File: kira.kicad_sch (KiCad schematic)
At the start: 41 parts, among them J1 USB_C_Receptacle_USB2.0, J2 SWD, SW37 SW_Push, U1 RP2040, U2 XC6206PxxxMR, U3 W25Q128JVS, U4 USBLC6-2SC6, Y1 12MHz

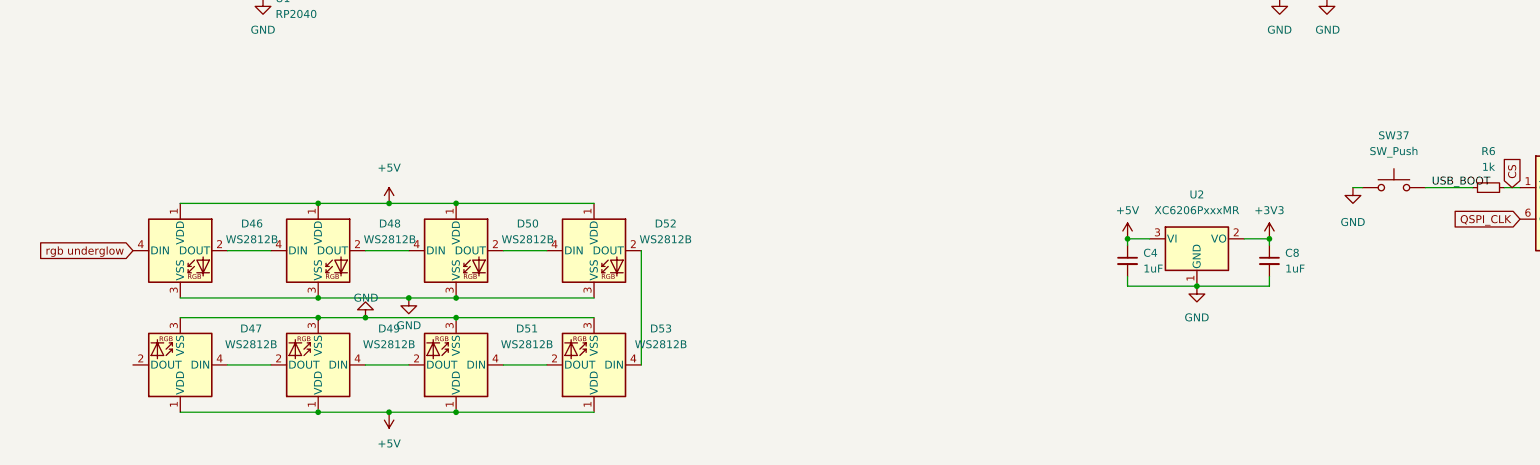
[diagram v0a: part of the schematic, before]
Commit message: removed underglow, cleaned some routing, fixed errors
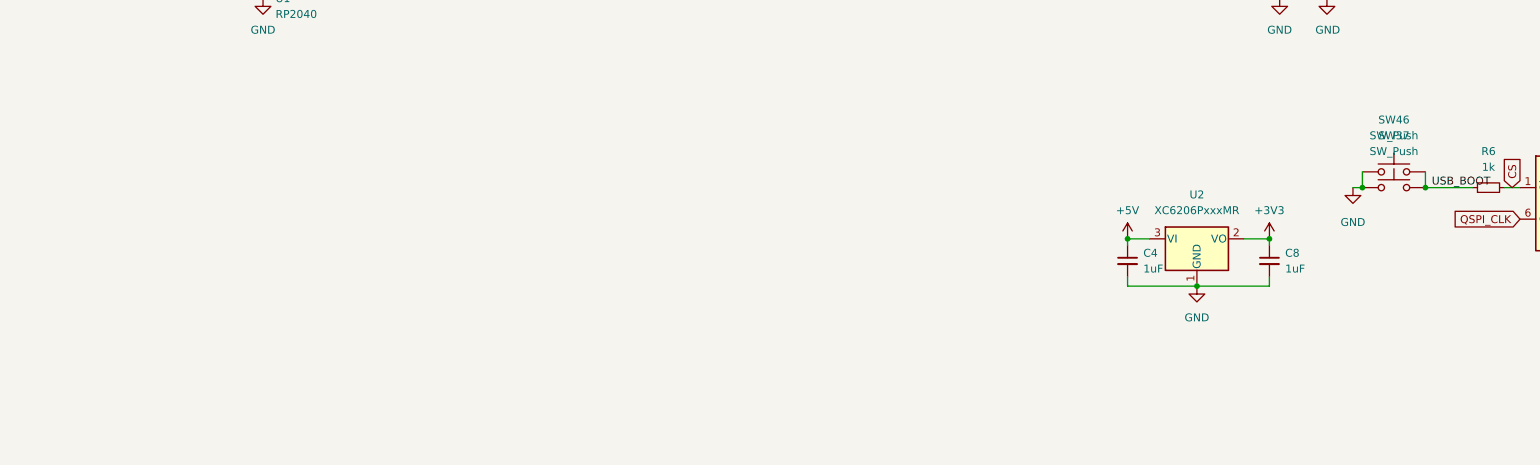
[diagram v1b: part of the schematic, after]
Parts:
- removed D46, D47, D48, D49, D50, D51, D52, D53: WS2812B, CrumpPrints:WS2812-2020, symbol LED:WS2812B
- added SW46: SW_Push, Keebio-Parts:SW_SPST_TL3342, symbol Switch:SW_Push
- SW37: footprint Connector_PinSocket_2.54mm:PinSocket_1x02_P2.54mm_Vertical -> Connector_PinHeader_2.00mm:PinHeader_1x02_P2.00mm_Vertical; now left out of the parts list
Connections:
- net GND: now also SW46.1
- net USB_BOOT: now also SW46.2

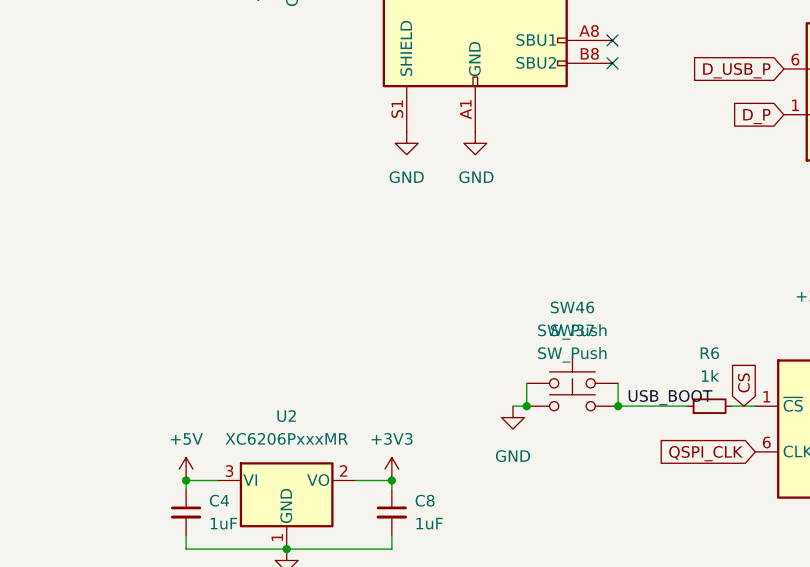
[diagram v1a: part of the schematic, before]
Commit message: silkscreen edited
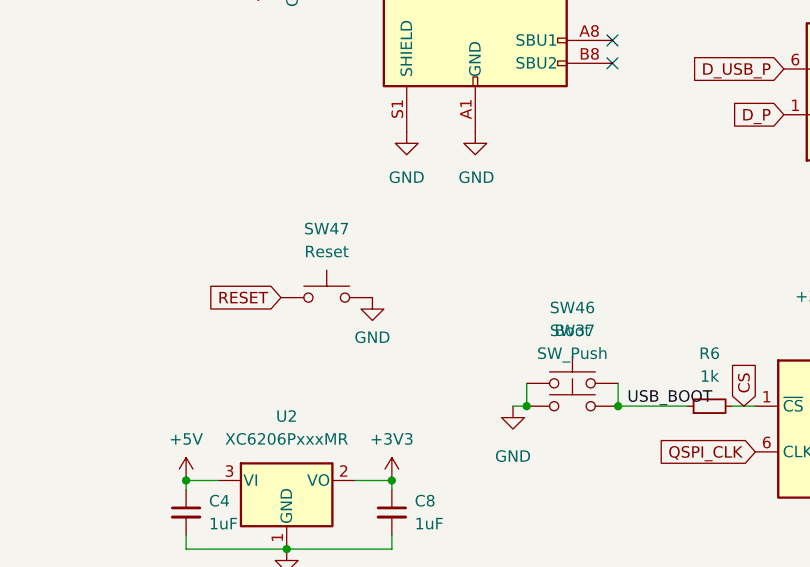
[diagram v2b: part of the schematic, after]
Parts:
- added SW47: Reset, Keebio-Parts:SW_SPST_TL3342, symbol Switch:SW_Push
- SW46: value SW_Push -> Boot
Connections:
- net GND: now also SW47.2
- net RESET: now also SW47.1
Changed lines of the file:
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@@
+    )
+  )
+  (global_label "RESET" (shape input) (at 196.215 133.35 180) (fields_autoplaced)
+    (effects (font (size 1.27 1.27)) (justify right))
+    (property "Intersheet References" "${INTERSHEET_REFS}" (id 0) (at 188.0567 133.2706 0)
+      (effects (font (size 1.27 1.27)) (justify right) hide)
     )
   )
@@
     )
     (property "Datasheet" "" (id 3) (at 217.805 114.935 0)
+      (effects (font (size 1.27 1.27)) hide)
+    )
+    (pin "1")
+  )
+  (symbol (lib_id "power:GND") (at 206.375 133.35 0) (unit 1)
+    (in_bom yes) (on_board yes) (fields_autoplaced)
+    (property "Reference" "#PWR0131" (id 0) (at 206.375 139.7 0)
+      (effects (font (size 1.27 1.27)) hide)
+    )
+    (property "Value" "GND" (id 1) (at 206.375 137.795 0))
+    (property "Footprint" "" (id 2) (at 206.375 133.35 0)
+      (effects (font (size 1.27 1.27)) hide)
+    )
+    (property "Datasheet" "" (id 3) (at 206.375 133.35 0)
       (effects (font (size 1.27 1.27)) hide)
     )
@@
     (pin "2")
   )
+  (symbol (lib_id "Switch:SW_Push") (at 201.295 133.35 0) (unit 1)
+    (in_bom yes) (on_board yes) (fields_autoplaced)
+    (property "Reference" "SW47" (id 0) (at 201.295 125.73 0))
+    (property "Value" "Reset" (id 1) (at 201.295 128.27 0))
+    (property "Footprint" "Keebio-Parts:SW_SPST_TL3342" (id 2) (at 201.295 128.27 0)
+      (effects (font (size 1.27 1.27)) hide)
+    )
+    (property "Datasheet" "~" (id 3) (at 201.295 128.27 0)
+      (effects (font (size 1.27 1.27)) hide)
+    )
+    (pin "1")
+    (pin "2")
+  )
   (symbol (lib_id "Device:C_Small") (at 185.674 157.226 0) (unit 1)
     (in_bom yes) (on_board yes) (fields_autoplaced)
@@
     (in_bom yes) (on_board yes) (fields_autoplaced)
     (property "Reference" "SW46" (id 0) (at 228.6 134.493 0))
-    (property "Value" "SW_Push" (id 1) (at 228.6 137.033 0))
+    (property "Value" "Boot" (id 1) (at 228.6 137.033 0))
     (property "Footprint" "Keebio-Parts:SW_SPST_TL3342" (id 2) (at 228.6 137.795 0)
       (effects (font (size 1.27 1.27)) hide)
@@
       (reference "#PWR0130") (unit 1) (value "GND") (footprint "")
     )
+    (path "/06dd8140-d842-4d91-a09d-19f94dcd5335"
+      (reference "#PWR0131") (unit 1) (value "GND") (footprint "")
+    )
     (path "/0ddedf06-cea5-4a1f-bea2-2a45031a82ea"
       (reference "C1") (unit 1) (value "1uF") (footprint "Capacitor_SMD:C_0402_1005Metric")
@@
     )
     (path "/c0879072-e435-401b-8624-0b44d019e717"
-      (reference "SW46") (unit 1) (value "SW_Push") (footprint "Keebio-Parts:SW_SPST_TL3342")
+      (reference "SW46") (unit 1) (value "Boot") (footprint "Keebio-Parts:SW_SPST_TL3342")
+    )
+    (path "/3fdd5214-4d43-4399-afca-8243e6545b7e"
+      (reference "SW47") (unit 1) (value "Reset") (footprint "Keebio-Parts:SW_SPST_TL3342")
     )
     (path "/f45907fd-0590-42cd-94d3-1afdfd6a497f"

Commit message: quick schematics cleanup
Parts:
- removed SW37: SW_Push, Connector_PinHeader_2.00mm:PinHeader_1x02_P2.00mm_Vertical, symbol Switch:SW_Push
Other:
- moved on the sheet: C1, C2, C3, C5, C6, R7, SW46, Y1

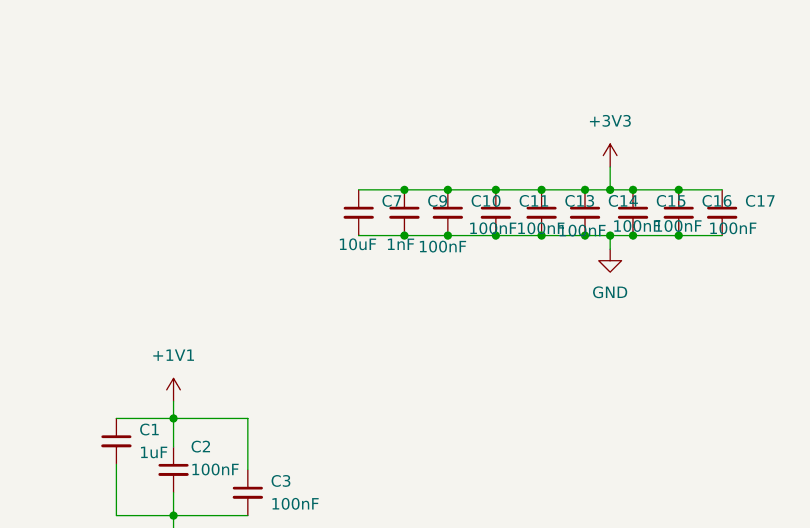
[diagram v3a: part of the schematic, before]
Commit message: started BOM, corrected schematic component value
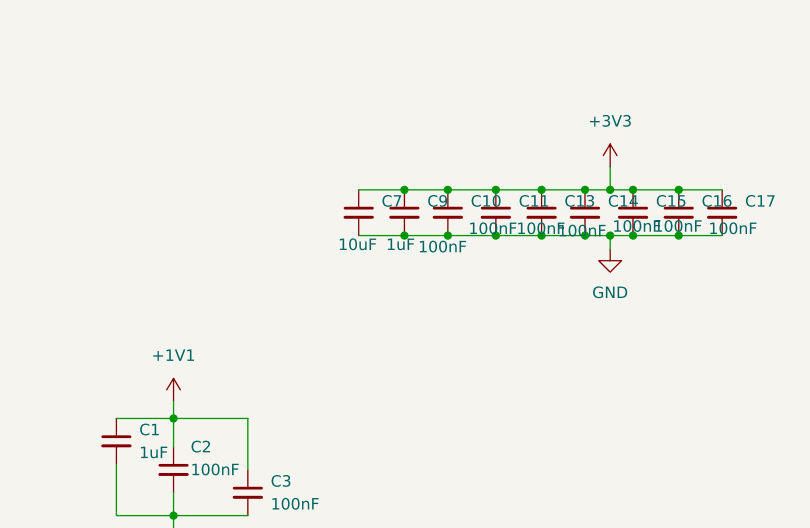
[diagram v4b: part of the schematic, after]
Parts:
- C9: value 1nF -> 1uF
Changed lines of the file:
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@@
       (effects (font (size 1.27 1.27)) (justify left))
     )
-    (property "Value" "1nF" (id 1) (at 151.257 34.671 0)
+    (property "Value" "1uF" (id 1) (at 151.257 34.671 0)
       (effects (font (size 1.27 1.27)) (justify left))
     )
@@
     )
     (path "/2d7efb7f-ebd2-47b3-9634-ae056645508c"
-      (reference "C9") (unit 1) (value "1nF") (footprint "Capacitor_SMD:C_0402_1005Metric")
+      (reference "C9") (unit 1) (value "1uF") (footprint "Capacitor_SMD:C_0402_1005Metric")
     )
     (path "/c945c869-566f-4554-8cf8-f76f7bb39da2"
